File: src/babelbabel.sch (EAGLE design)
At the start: 83 parts, among them CON1 CON-4P-TABS-JST_GH-RA, CON10 CON-6P-SM06B, CON11 PINHEAD_1X04-2.54, CON12 PINHEAD_1X06-2.54, CON15 PINHEAD_1X04-2.54, CON16 CON-4P-TABS-JST_GH-RA, CON2 PINHEAD_1X04-2.54, CON3 PINHEAD_1X04-2.54, CON4 USB-AA-PTH, CON5 CON-4P-TABS-JST_GH-RA, CON6 CON-4P-TABS-JST_GH-RA, CON7 USB-1, IC13 STM32F103CBT7, IC14 74LVC2T45, IC15 74LVC2T45, IC16 74LVC2T45, IC17 74LVC2T45, IC3 AP2127-3.3, IC9 FE1.1S, J1 CONNECTION-SMD, J2 CONNECTION-SMD, Q10 DMG1024UV-7, Q8 16MHz, Q9 DMG1023UV-7

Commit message: Routing seems done
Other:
- note added: "Find out what's going on with XRST IRST Check other ERC errors"
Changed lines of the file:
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@@
 <attribute name="TOLERANCE" x="136.652" y="61.214" size="0.762" layer="96" font="vector" rot="R90"/>
 </instance>
-<instance part="R11" gate="G$1" x="86.36" y="144.78" smashed="yes" rot="R270">
-<attribute name="NAME" x="86.36" y="144.78" size="1.27" layer="95" font="vector" rot="R270" align="center"/>
-<attribute name="VALUE" x="84.328" y="145.034" size="0.762" layer="96" font="vector" rot="R270" align="bottom-right"/>
-<attribute name="PACKAGE" x="86.868" y="148.59" size="0.508" layer="95" font="vector" rot="R270" align="center"/>
-<attribute name="TOLERANCE" x="84.328" y="144.526" size="0.762" layer="96" font="vector" rot="R270"/>
+<instance part="R11" gate="G$1" x="86.36" y="147.32" smashed="yes" rot="R270">
+<attribute name="NAME" x="86.36" y="147.32" size="1.27" layer="95" font="vector" rot="R270" align="center"/>
+<attribute name="VALUE" x="84.328" y="147.574" size="0.762" layer="96" font="vector" rot="R270" align="bottom-right"/>
+<attribute name="PACKAGE" x="86.868" y="151.13" size="0.508" layer="95" font="vector" rot="R270" align="center"/>
+<attribute name="TOLERANCE" x="84.328" y="147.066" size="0.762" layer="96" font="vector" rot="R270"/>
 </instance>
 <instance part="Q1" gate="P" x="40.64" y="116.84" smashed="yes" rot="R90">
@@
 <attribute name="VALUE" x="111.76" y="82.296" size="1.27" layer="96" font="vector" ratio="15" align="center"/>
 </instance>
-<instance part="GND2" gate="1" x="86.36" y="154.94" smashed="yes" rot="R180">
-<attribute name="VALUE" x="86.36" y="156.21" size="1.27" layer="96" font="vector" ratio="15" rot="R180" align="center"/>
+<instance part="GND2" gate="1" x="86.36" y="157.48" smashed="yes" rot="R180">
+<attribute name="VALUE" x="86.36" y="158.75" size="1.27" layer="96" font="vector" ratio="15" rot="R180" align="center"/>
 </instance>
 <instance part="GND48" gate="1" x="48.26" y="116.84" smashed="yes" rot="R90">
@@
 <net name="BOOT0" class="0">
 <segment>
-<wire x1="86.36" y1="137.16" x2="86.36" y2="139.7" width="0.1524" layer="91"/>
+<wire x1="86.36" y1="137.16" x2="86.36" y2="142.24" width="0.1524" layer="91"/>
 <pinref part="IC1" gate="G$1" pin="BOOT0"/>
 <pinref part="R11" gate="G$1" pin="2"/>
@@
 </segment>
 <segment>
-<wire x1="86.36" y1="152.4" x2="86.36" y2="149.86" width="0.1524" layer="91"/>
+<wire x1="86.36" y1="154.94" x2="86.36" y2="152.4" width="0.1524" layer="91"/>
 <pinref part="R11" gate="G$1" pin="1"/>
 <pinref part="GND2" gate="1" pin="GND"/>
@@
 </segment>
 </net>
-<net name="N$17" class="0">
-<segment>
-<pinref part="IC2" gate="G$1" pin="VREF+"/>
-<wire x1="-76.2" y1="83.82" x2="-76.2" y2="81.28" width="0.1524" layer="91"/>
-</segment>
-</net>
-<net name="N$1" class="0">
-<segment>
-<pinref part="IC1" gate="G$1" pin="PB14"/>
-<wire x1="116.84" y1="99.06" x2="119.38" y2="99.06" width="0.1524" layer="91"/>
-</segment>
-</net>
 <net name="PA5" class="0">
 <segment>
@@
 </segment>
 </net>
-<net name="N$5" class="0">
-<segment>
-<pinref part="IC1" gate="G$1" pin="PB7"/>
-<wire x1="88.9" y1="137.16" x2="88.9" y2="139.7" width="0.1524" layer="91"/>
-</segment>
-</net>
-<net name="N$6" class="0">
-<segment>
-<pinref part="IC1" gate="G$1" pin="PB6"/>
-<wire x1="91.44" y1="137.16" x2="91.44" y2="139.7" width="0.1524" layer="91"/>
-</segment>
-</net>
 </nets>
 </sheet>
@@
 <wire x1="175.26" y1="25.4" x2="254" y2="25.4" width="0.1524" layer="97" style="shortdash"/>
 <wire x1="254" y1="25.4" x2="254" y2="78.74" width="0.1524" layer="97" style="shortdash"/>
+<text x="129.54" y="-17.78" size="5.08" layer="97">Find out what's going on with XRST IRST
+Check other ERC errors</text>
 </plain>
 <instances>
 <instance part="FRAME4" gate="G$1" x="0" y="0" smashed="yes">
-<attribute name="DRAWING_NAME" x="217.17" y="17.78" size="2.54" layer="94"/>
-<attribute name="LAST_DATE_TIME" x="217.17" y="12.7" size="2.286" layer="94"/>
+<attribute name="DRAWING_NAME" x="217.17" y="15.24" size="2.54" layer="94"/>
+<attribute name="LAST_DATE_TIME" x="217.17" y="10.16" size="2.286" layer="94"/>
 <attribute name="SHEET" x="230.505" y="5.08" size="2.54" layer="94"/>
 </instance>
@@
 </sheet>
 </sheets>
+<errors>
+</errors>
 </schematic>
 </drawing>

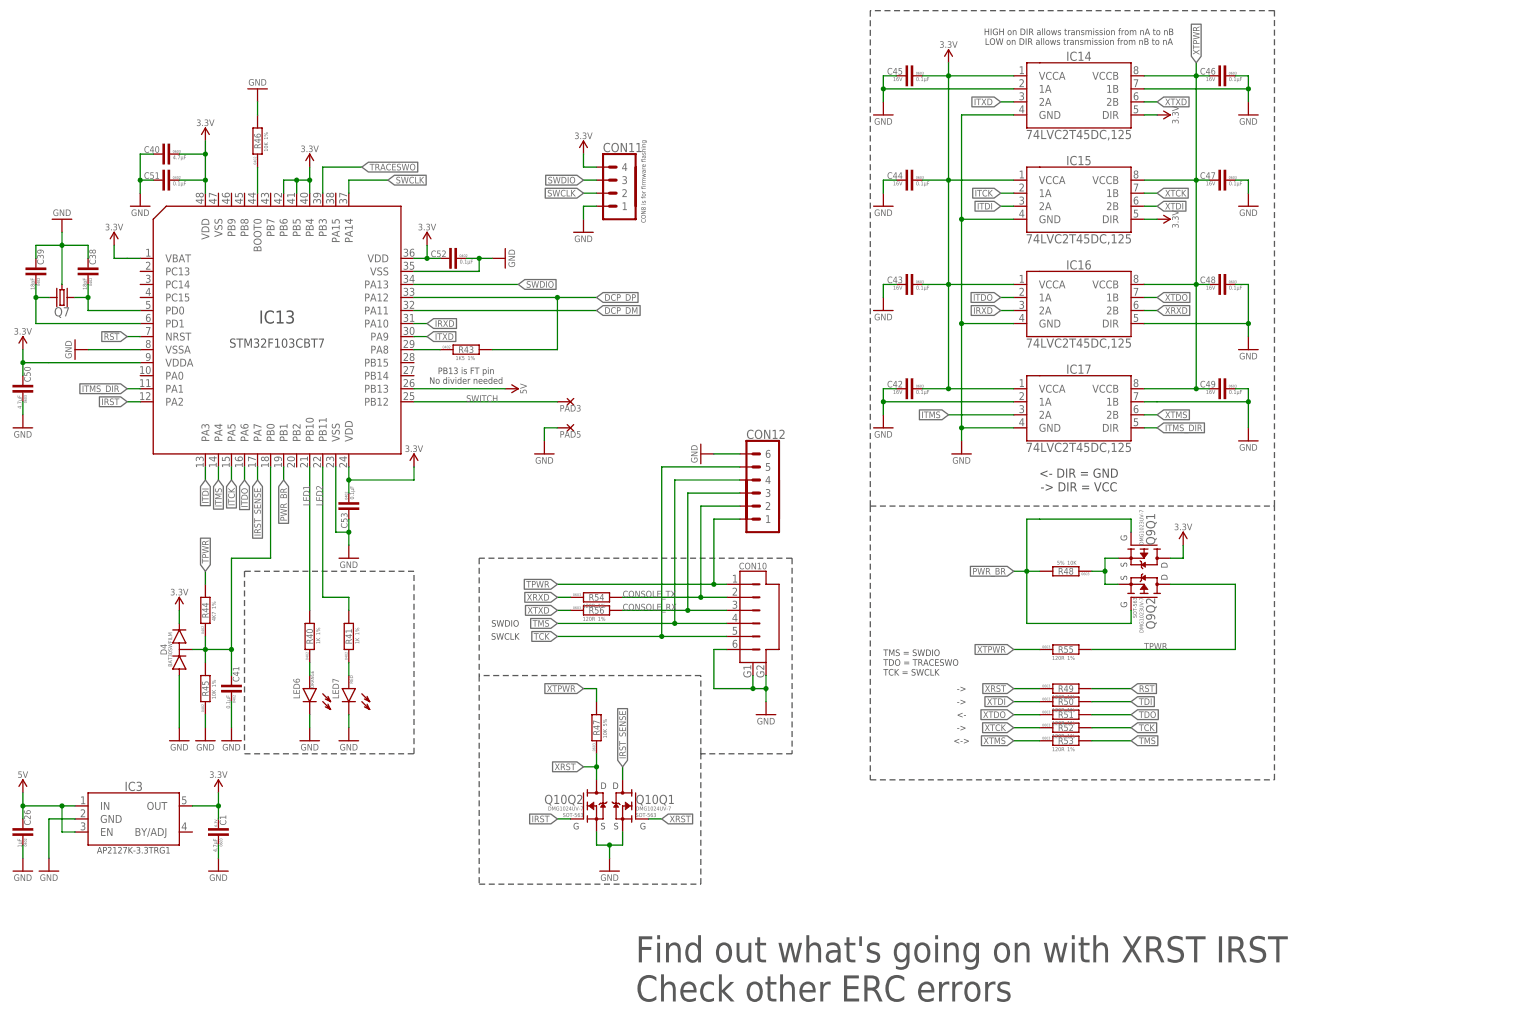
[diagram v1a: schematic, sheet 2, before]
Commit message: excessive DCP nets removed
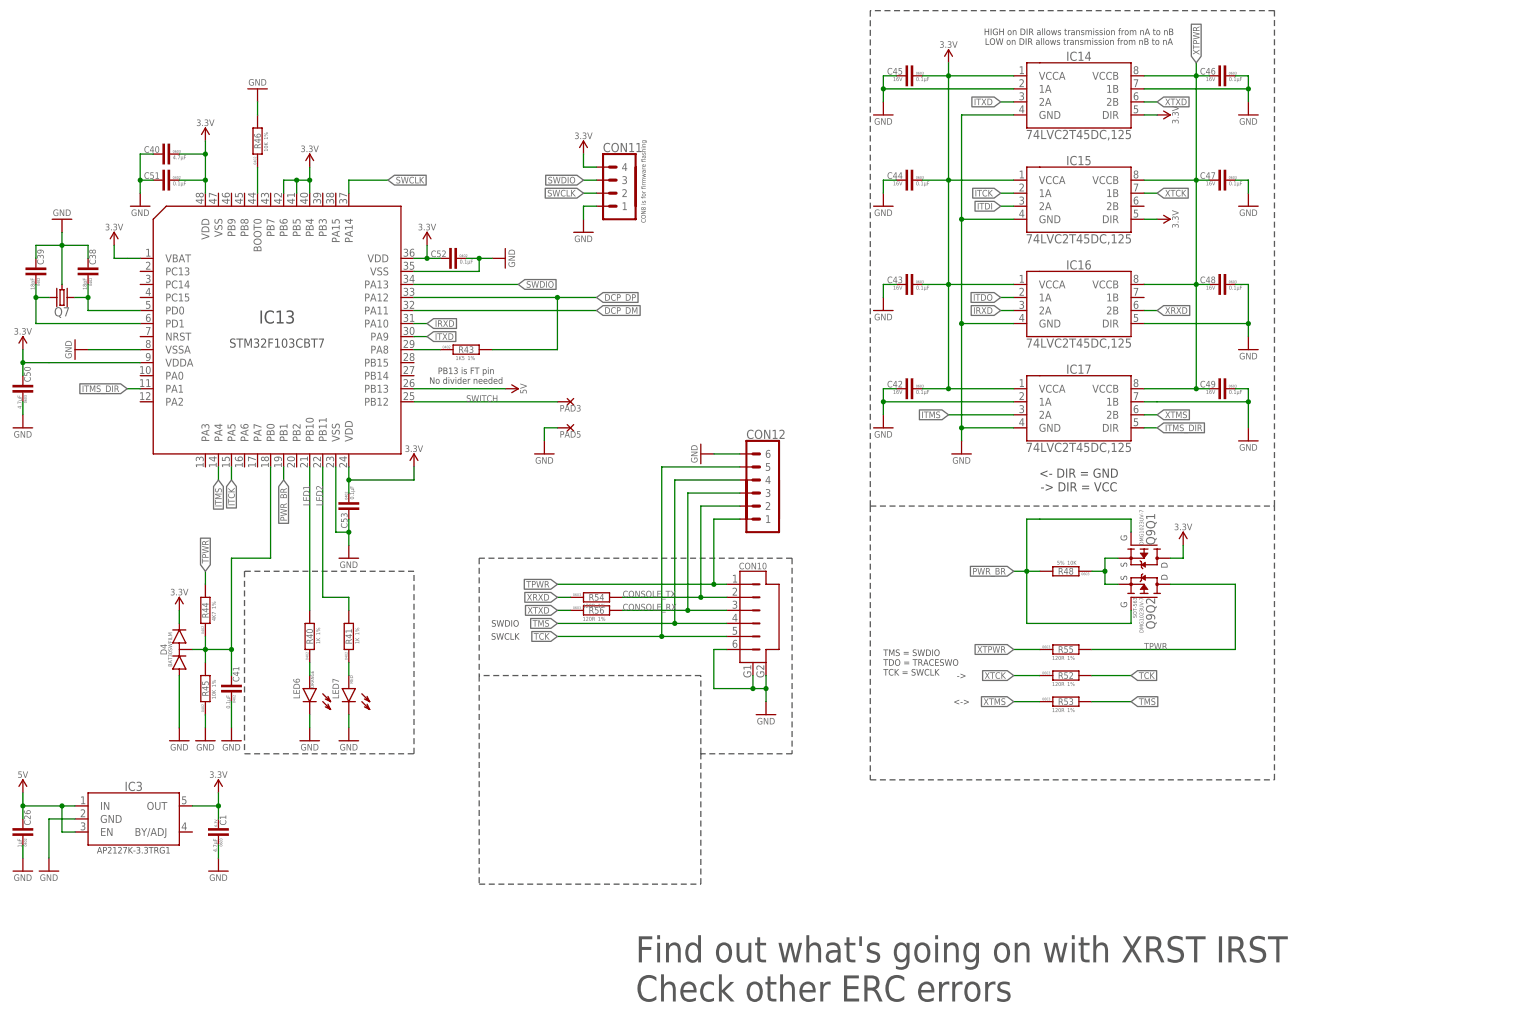
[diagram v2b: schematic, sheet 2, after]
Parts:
- removed Q10: DMG1024UV-7, mosfet:DMG1024UV-7
- removed R47: 10K, R_digikey:10K-5%-0603
- removed R49, R50, R51: 120R, R_digikey:120R-1%-0603
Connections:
- removed net !RST: IC13.NRST
- removed net IRST: IC13.PA2, Q10Q2.G
- removed net IRST_SENSE: IC13.PA7, Q10Q1.D
- removed net RST: R49.2
- removed net TDI: R50.2
- removed net TDO: R51.2
- removed net TRACESWO: IC13.PB3
- removed net XRST: Q10Q1.G, Q10Q2.D, R47.1, R49.1
- removed net XTDI: IC15.2B, R50.1
- removed net XTDO: IC16.1B, R51.1
- net GND: no longer Q10Q1.S, Q10Q2.S
- net ITDI: no longer IC13.PA3
- net ITDO: no longer IC13.PA6
- net XTPWR: no longer R47.2
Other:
- note removed: "<-"
- moved on the sheet: R52, R53

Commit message: SSOP28 footprint update
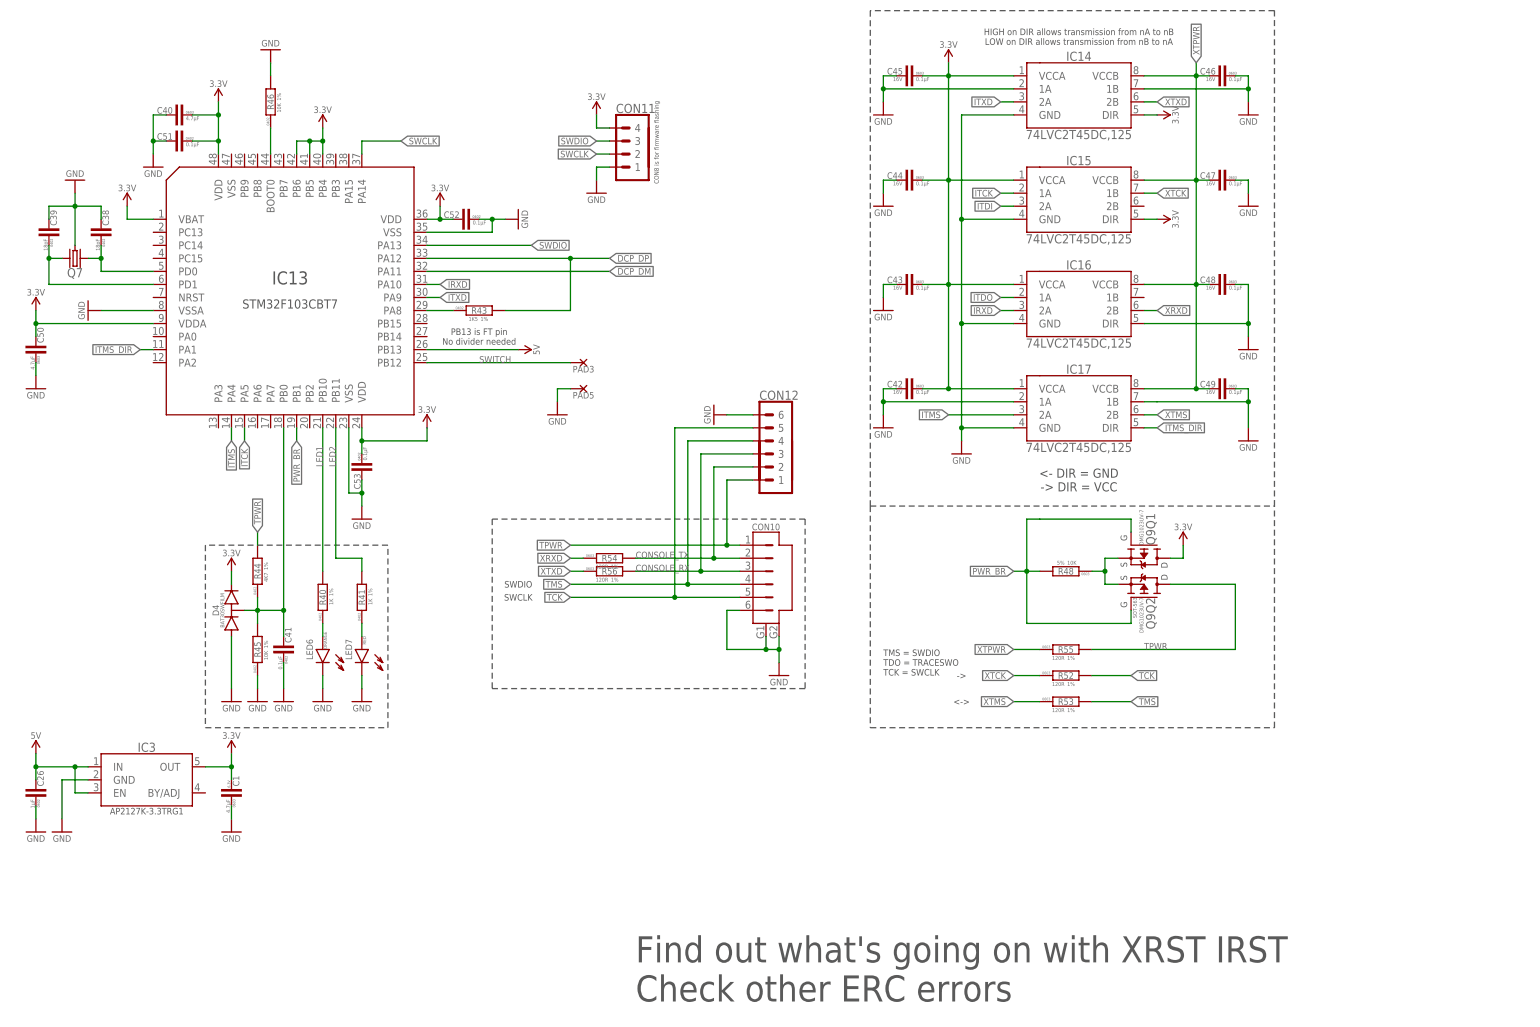
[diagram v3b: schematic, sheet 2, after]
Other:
- moved on the sheet: C1, C26, C38, C39, C40, C41, C50, C51, C52, C53, CON10, CON11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

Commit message: All doubtful issues resolved
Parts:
- Q9: value DMG1023UV-7 -> NTZD3152PT1G; device mosfet:DMG1023UV-7 -> mosfet:NTZD3152PT1G
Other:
- note removed: "Find out what's going on with XRST IRST Check other ERC errors"
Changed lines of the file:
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@@
 <?xml version="1.0" encoding="utf-8"?>
 <!DOCTYPE eagle SYSTEM "eagle.dtd">
-<eagle version="9.6.2">
+<eagle version="9.6.0">
 <drawing>
 <settings>
@@
 <part name="P+10" library="supply_symbols" library_urn="urn:adsk.eagle:library:5017758" deviceset="3.3V" device=""/>
 <part name="R1" library="rc" library_urn="urn:adsk.eagle:library:2539423" deviceset="R" device="-0402" package3d_urn="urn:adsk.eagle:package:2539456/2" technology="-1%" value="10K"/>
-<part name="IC2" library="stm32" library_urn="urn:adsk.eagle:library:2473361" deviceset="STM32F373RCT6" device="" package3d_urn="urn:adsk.eagle:package:2473349/4"/>
+<part name="IC2" library="stm32" library_urn="urn:adsk.eagle:library:2473361" deviceset="STM32F373RCT6" device="" package3d_urn="urn:adsk.eagle:package:2473349/4">
+<attribute name="DIGIKEY#" value="497-13252-ND"/>
+</part>
 <part name="P+11" library="supply_symbols" library_urn="urn:adsk.eagle:library:5017758" deviceset="3.3V" device=""/>
 <part name="P+12" library="supply_symbols" library_urn="urn:adsk.eagle:library:5017758" deviceset="3.3V" device=""/>
@@
 <part name="R46" library="rc" library_urn="urn:adsk.eagle:library:2539423" deviceset="R" device="-0402" package3d_urn="urn:adsk.eagle:package:2539456/2" technology="-1%" value="10K"/>
 <part name="GND86" library="supply_symbols" library_urn="urn:adsk.eagle:library:5017758" deviceset="GND" device="" value="GND"/>
-<part name="Q9" library="mosfet" library_urn="urn:adsk.eagle:library:2640523" deviceset="DMG1023UV-7" device="" package3d_urn="urn:adsk.eagle:package:8711362/3"/>
+<part name="Q9" library="mosfet" library_urn="urn:adsk.eagle:library:2640523" deviceset="NTZD3152PT1G" device="" package3d_urn="urn:adsk.eagle:package:8711362/3"/>
 <part name="R48" library="R_digikey" library_urn="urn:adsk.eagle:library:2539499" deviceset="10K" device="-0603" package3d_urn="urn:adsk.eagle:package:2539515/2" technology="-5%" value="10K"/>
 <part name="+P37" library="supply_symbols" library_urn="urn:adsk.eagle:library:5017758" deviceset="3.3V" device=""/>
@@
 <wire x1="175.26" y1="35.56" x2="254" y2="35.56" width="0.1524" layer="97" style="shortdash"/>
 <wire x1="254" y1="35.56" x2="254" y2="78.74" width="0.1524" layer="97" style="shortdash"/>
-<text x="129.54" y="-17.78" size="5.08" layer="97">Find out what's going on with XRST IRST
-Check other ERC errors</text>
 </plain>
 <instances>

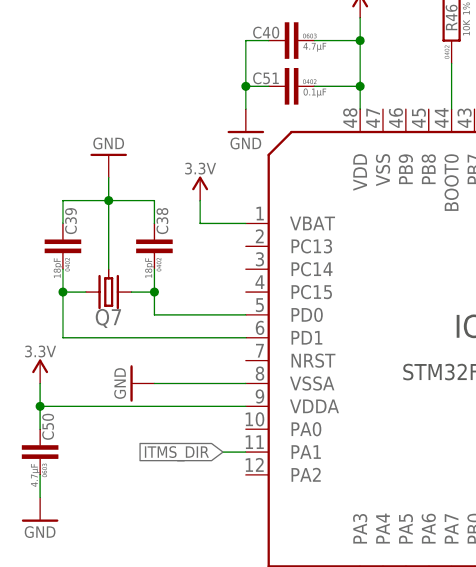
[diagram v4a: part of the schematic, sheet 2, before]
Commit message: CAN transciever replaced
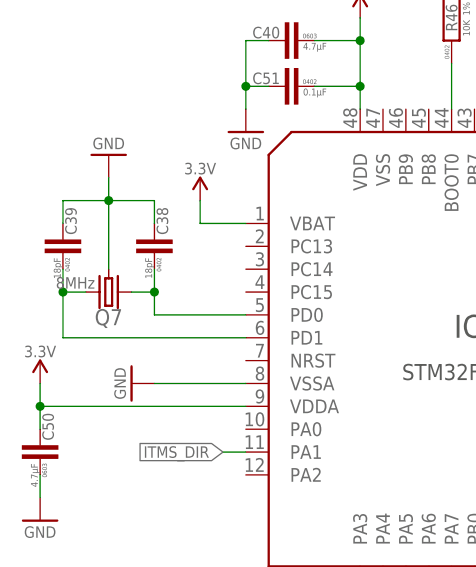
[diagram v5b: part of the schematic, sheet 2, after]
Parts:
- IC3: LCSC# C156285 -> (none)
- Q7: value (none) -> 8MHz
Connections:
- net VDD_3V3: no longer C5.2
- net VDD_5V: now also C5.2

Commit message: Babel part attributes added
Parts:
- IC13: LCSC# (none) -> C8304
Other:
- note removed: "C1, C2, C14 can be excluded."
- note removed: "R1, R2 may be replaced with solder joints"
- moved on the sheet: C31, C32, C33, C5, C7, CON15, CON4, CON7, D3, IC9, PAD1, PAD2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

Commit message: Massive attribute update
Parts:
- C1: value 4.7µF -> 4.7uF; AEC-Q --- -> (none); DIGIKEY# 1276-2087-1-ND -> (none); LCSC# (none) -> C19666; MANF Samsung Electro-Mechanics -> (none); MANF# CL10B475KQ8NQNC -> (none); OPERATING_TEMP -55°C ~ 125°C -> (none); VOLTAGE 6.3V -> (none)
- C26: value 1µF -> 1uF; LCSC# (none) -> C52923
- C31, C5, C7: LCSC# (none) -> C15850; VOLTAGE 6.3V -> (none)
- C32, C33: value 18pF -> 20pF; LCSC# (none) -> C1554; VOLTAGE 50V -> (none)
- C38, C39: value 18pF -> 10pF; LCSC# (none) -> C32949
- C40, C50: value 4.7µF -> 4.7uF; LCSC# (none) -> C19666
- C41, C51, C52, C53: value 0.1µF -> 0.1uF; LCSC# (none) -> C1525
- C42, C43, C44, C45, C46, C47, C48, C49: value 0.1µF -> 0.1uF; device C_digikey:0.1µF-16V_10%_X7R-0603 -> rc:C-0402; LCSC# (none) -> C1525
- IC14: LCSC# (none) -> C139382
- LED6: COLOR ORANGE -> GREEN; DIGIKEY# 160-1445-1-ND -> (none); LCSC# (none) -> C74338
- LED7: DIGIKEY# SML-D12U1WT86CT-ND -> (none); LCSC# (none) -> C74339
- Q7: LCSC# (none) -> C133366; LOAD_CAPACITANCE (none) -> 10pF
- Q8: ESR 80Ω -> (none); LCSC# C9002 -> C164049; MANF Yangxing Tech -> (none); MANF# X322512MSB4SI -> (none)
- R1, R2: value 100K -> 120R; device rc:R-1%-0402 -> rc:R-1%-0603; LCSC# (none) -> C22787
- R10, R6, R9: LCSC# (none) -> C25803
- R40, R41: LCSC# (none) -> C11702
- R43: DIGIKEY# 311-1.50KHRCT-ND -> (none); LCSC# (none) -> C25867; MANF Yageo -> (none); MANF# RC0603FR-071K5L -> (none)
- R44: LCSC# (none) -> C25900
- R45, R46: LCSC# (none) -> C25744
- R48: device R_digikey:10K-5%-0603 -> rc:R-1%-0402; LCSC# (none) -> C25744
- R5: LCSC# (none) -> C13167
- R52, R53, R55: device R_digikey:120R-1%-0603 -> rc:R-1%-0603; LCSC# (none) -> C22787
- R54, R56: device R_digikey:120R-1%-0603 -> rc:R-1%-0402; LCSC# (none) -> C25079
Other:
- moved on the sheet: C39, Q7

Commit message: BOM improvement
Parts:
- D4: value BAT30SWFILM -> BAT54SWT1G; device Diodes:BAT30SWFILM -> Diodes:BAT54SWT1G
- Q8: value 16MHz -> 12MHz; LCSC# C164049 -> C9002
- R54, R56: device rc:R-1%-0402 -> rc:R-1%-0603; LCSC# C25079 -> C22787
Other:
- moved on the sheet: R54, R56
